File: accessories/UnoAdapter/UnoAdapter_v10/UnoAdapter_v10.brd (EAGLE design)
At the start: 71.1 x 52.7 mm, 26 parts, among them IC1 7805, X1 DC21MMX

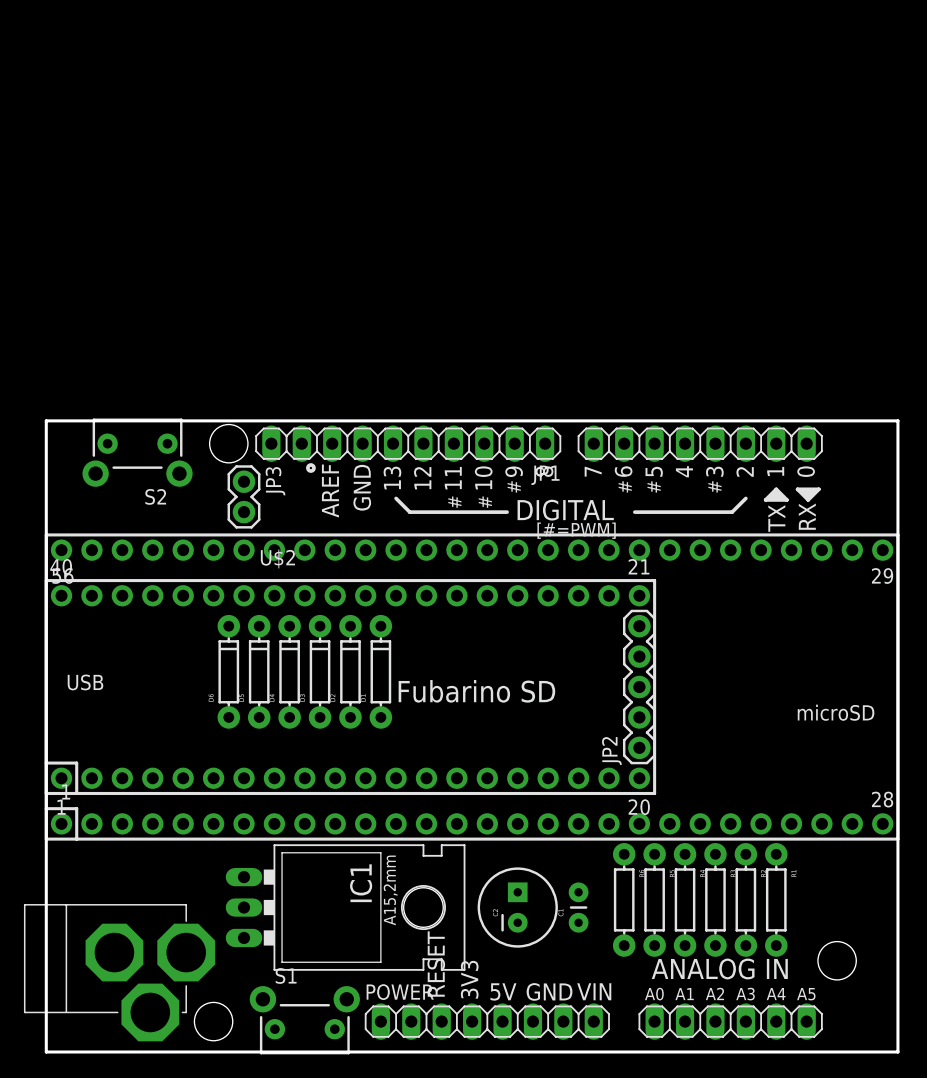
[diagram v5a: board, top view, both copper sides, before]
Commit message: First rough draft of schematic done, first super crappy routing done.
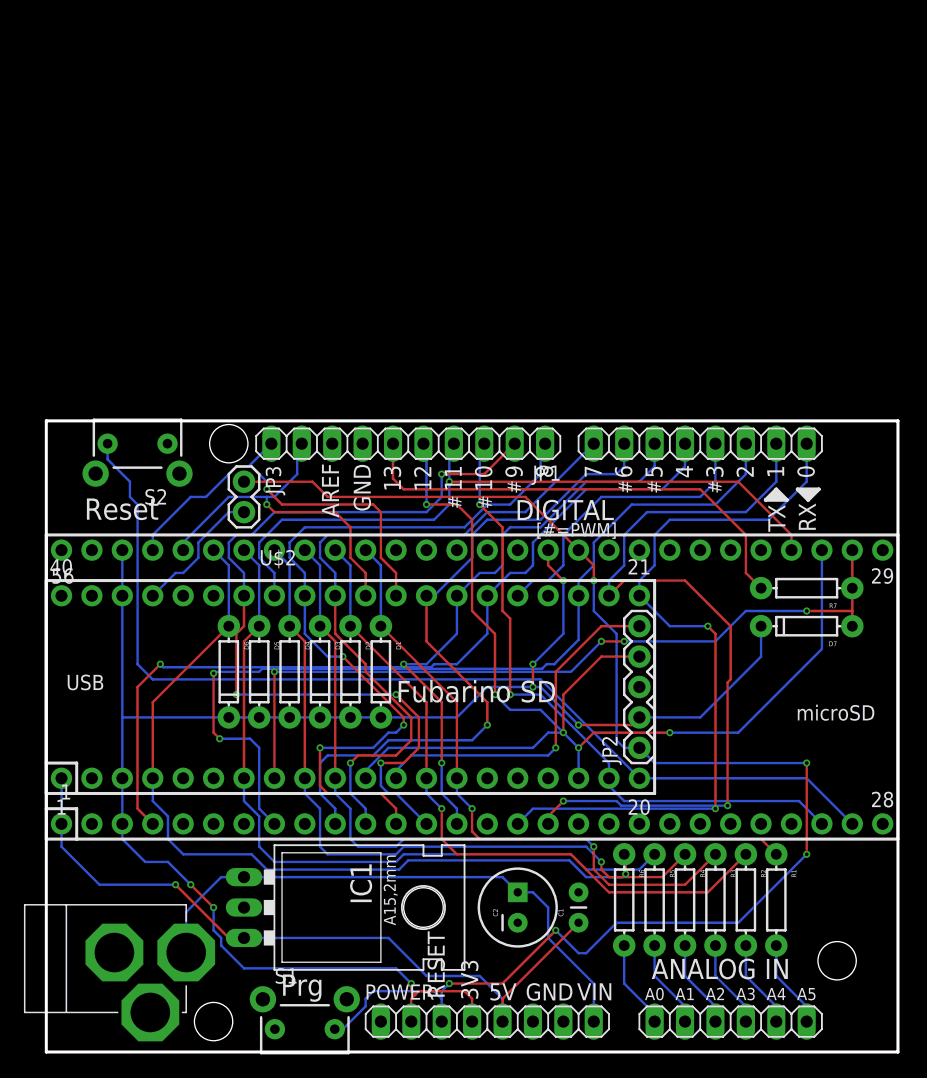
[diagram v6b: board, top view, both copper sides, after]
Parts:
- added D7: (no value), SparkFun-DiscreteSemi:DIODE-1N4148
- added R7: (no value), SparkFun-Passives:AXIAL-0.3
- turned D1 to 270 degrees
- turned D2 to 270 degrees
- turned D3 to 270 degrees
- turned D4 to 270 degrees
- turned D5 to 270 degrees
- turned D6 to 270 degrees
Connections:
- removed net N$27: U$1.26
- removed net N$32: U$2.34
- removed net N$45: U$2.33
- removed net N$46: U$2.32
- removed net N$47: U$2.31
- removed net N$57: U$2.30
- removed net N$58: U$2.29
- removed net N$59: U$2.28
- removed net N$60: U$2.27
- removed net N$61: U$2.26
- removed net N$62: U$2.25
- removed net N$64: U$2.23
- removed net N$65: U$2.22
- removed net N$66: U$2.21
- removed net N$70: U$2.4
- removed net N$73: U$2.7
- removed net N$74: U$2.8
- removed net N$75: U$2.9
- removed net N$76: U$2.10
- removed net N$79: U$2.13
- removed net N$80: U$2.14
- removed net N$84: U$2.18
- removed net N$85: U$2.19
- new net $123: JP1.6, R7.P$2
- new net SS_SD: U$1.33
- net +3V3: now also D7.C
- net AD0: now also U$2.4
- net AD1: now also U$2.7
- net AD2: now also U$2.9
- net AD3: now also U$2.10
- net AD4: now also U$2.13
- net AD4/SDA: now also U$2.30
- net AD5: now also U$2.14
- net AD5/SCL: now also U$2.29
- net IO0: now also U$2.21
- net IO1: now also U$2.22
- net IO2: now also U$2.23
- net IO3: now also U$2.25
- net IO4: now also U$2.26
- net IO5: now also U$2.27
- net IO6: now also U$2.28
- net IO7: now also U$2.31
- net IO8: now also U$2.32
- net IO9: now also U$2.34
- net MISO: now also U$2.18
- net MOSI: now also U$2.33
- net SCK: now also D7.A, R7.P$1, U$2.8; no longer JP1.6
- net SS: now also U$1.26, U$2.19; no longer U$1.33
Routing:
- net +3V3: track 0.00 -> 138.9 mm, vias 0 -> 7
- net RESET: track 0.00 -> 122.0 mm, vias 0 -> 5
- net PRG: track 0.00 -> 84.7 mm
- net IO2: track 0.00 -> 74.1 mm, vias 0 -> 2
- net IO9: track 0.00 -> 71.2 mm, vias 0 -> 4
- net IO4: track 0.00 -> 70.4 mm, vias 0 -> 1
- net AD0: track 0.00 -> 69.8 mm, vias 0 -> 1
- net MISO: track 0.00 -> 68.3 mm, vias 0 -> 4
- net IO1: track 0.00 -> 67.0 mm, vias 0 -> 2
- net SCK: track 0.00 -> 65.6 mm, vias 0 -> 4
- net IO8: track 0.00 -> 65.3 mm, vias 0 -> 3
- net IO0: track 0.00 -> 62.6 mm, vias 0 -> 2
- net AD1: track 0.00 -> 61.2 mm
- net +5V: track 0.00 -> 60.6 mm, vias 0 -> 1
- net AD3: track 0.00 -> 60.5 mm, vias 0 -> 1
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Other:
- board text added: "Prg"
- board text added: "Reset"
